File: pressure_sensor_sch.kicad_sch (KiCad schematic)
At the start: 54 parts, among them J13 1053131104, U7 ADS131M06IPBS

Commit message: Most Review 1 changes made
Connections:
- net GND: now also U7.22 (XTAL2)
- no-connect marks 3 -> 2
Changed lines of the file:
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@@
   (junction (at 221.996 125.984) (diameter 0) (color 0 0 0 0)
   )
-  (no_connect (at 98.298 106.68))
   (no_connect (at 98.298 116.84))
   (no_connect (at 32.258 114.3))
@@
         )
       )
+    )
+  )
+  (symbol (lib_name "GND_1") (lib_id "power:GND") (at 98.298 106.68 0) (unit 1)
+    (in_bom yes) (on_board yes) (dnp no) (fields_autoplaced)
+    (property "Reference" "#PWR0181" (at 98.298 113.03 0)
+      (effects (font (size 1.27 1.27)) hide)
+    )
+    (property "Value" "GND" (at 98.298 111.506 0)
+      (effects (font (size 1.27 1.27)) hide)
+    )
+    (property "Footprint" "" (at 98.298 106.68 0)
+      (effects (font (size 1.27 1.27)) hide)
+    )
+    (property "Datasheet" "" (at 98.298 106.68 0)
+      (effects (font (size 1.27 1.27)) hide)
+    )
+    (pin "1")
+    (instances
+      (project "Ricardo-Stark"
+        (path "/7db990e4-92e1-4f99-b4d2-435bbec1ba83/249a9f46-b59f-4de1-97d1-386ac76339a5"
+          (reference "#PWR0181") (unit 1)
+        )
+      )

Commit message: Review 1 Changes Complete
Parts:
- removed C39: 220nF, Capacitor_SMD:C_0402_1005Metric, symbol Device:C_Small
- removed C39: 1uF, Capacitor_SMD:C_0402_1005Metric, symbol Device:C_Small
- added C41: 0.1uF, Capacitor_SMD:C_0402_1005Metric, symbol Device:C_Small
- added C43: 220nF, Capacitor_SMD:C_0402_1005Metric, symbol Device:C_Small
- added C46: 1uF, Capacitor_SMD:C_0402_1005Metric, symbol Device:C_Small
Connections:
- net +3.3V: now also C41.1, C46.1
- net GND: now also C41.2, C43.2, C46.2
- net at U7.24 (CAP): now also C43.1
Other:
- moved on the sheet: JP39, R61

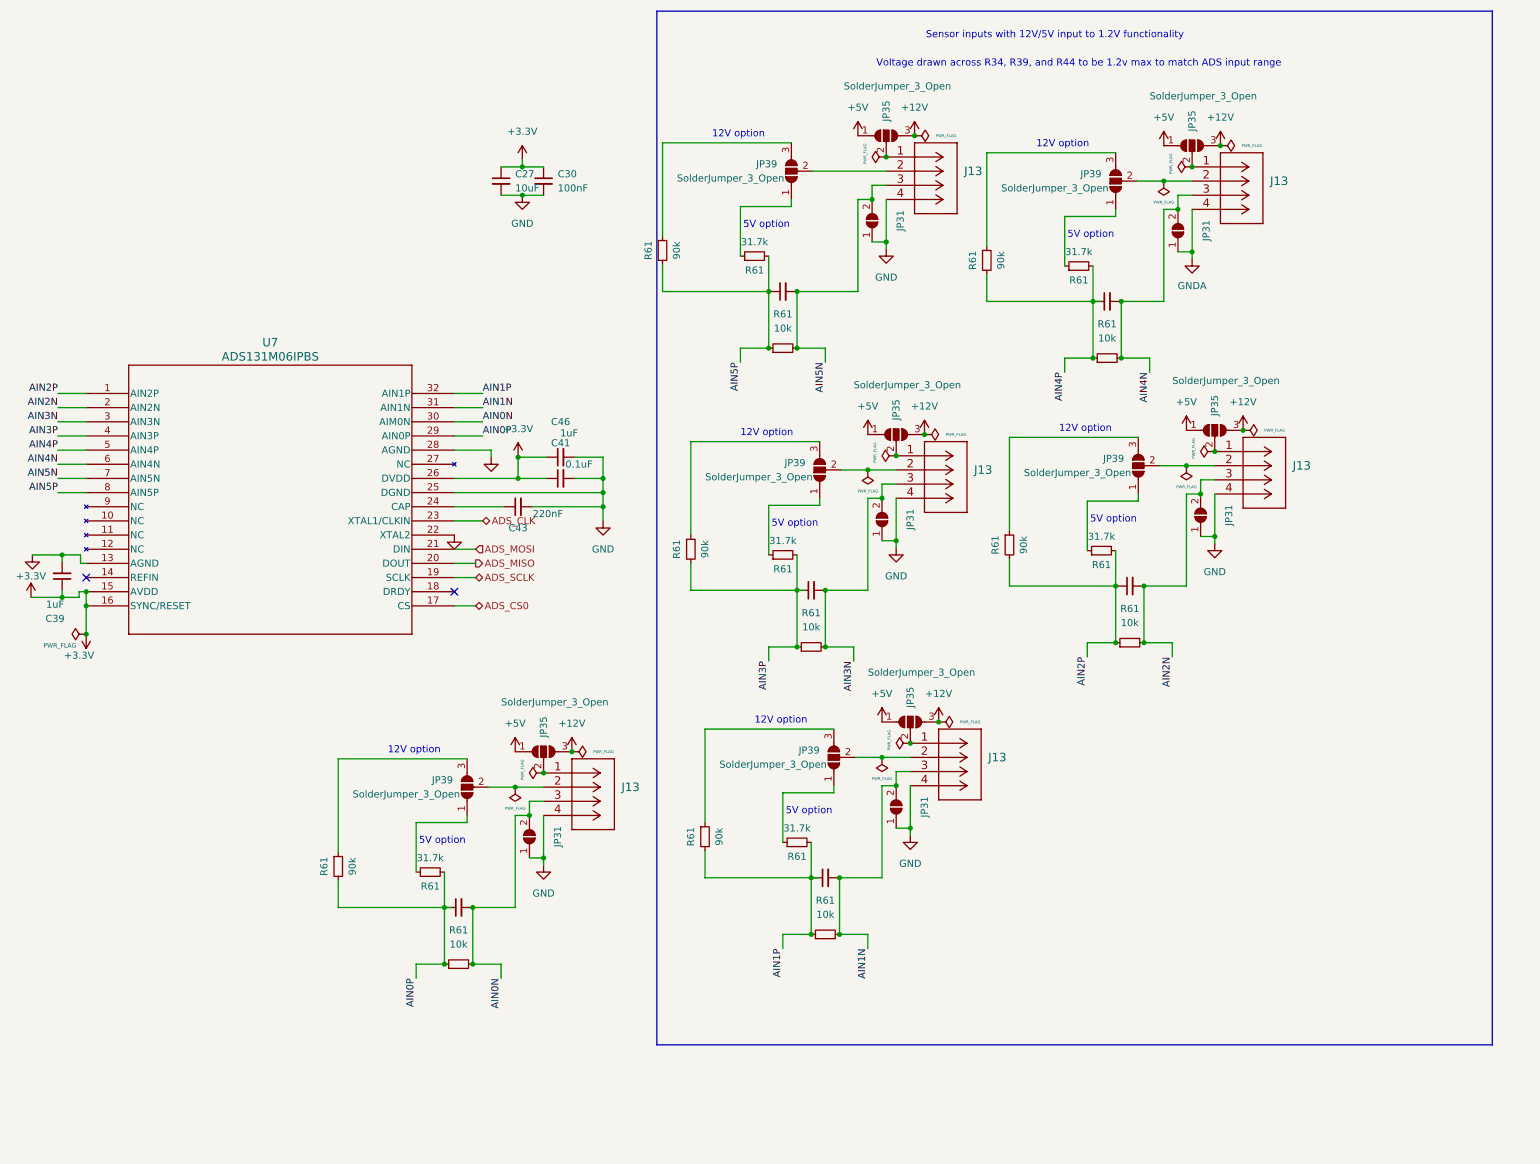
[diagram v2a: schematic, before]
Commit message: Sized sensor resistors and more routing
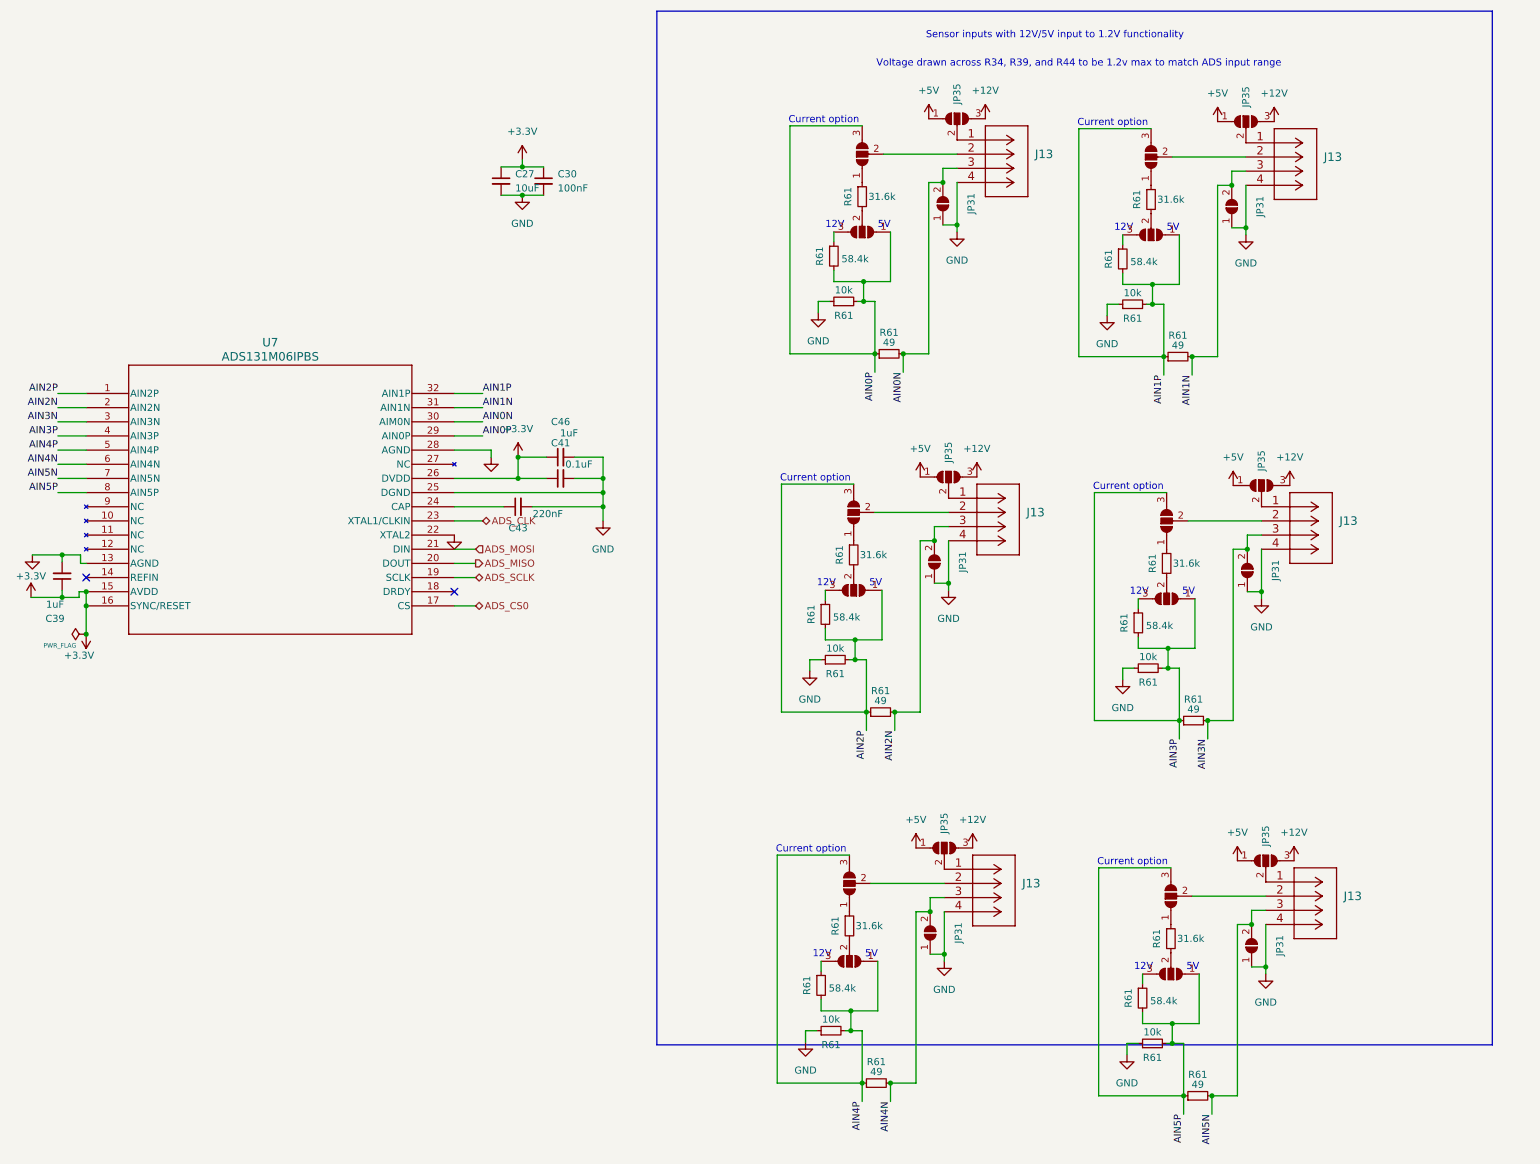
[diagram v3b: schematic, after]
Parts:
- removed C73 (x6): 10nF, Capacitor_SMD:C_0402_1005Metric, symbol Device:C_Small
- removed J13 (x5): 1053131104, Connector_Molex:Molex_Nano-Fit_105313-xx04_1x04_P2.50mm_Horizontal, symbol iclr:1053131104
- removed JP31 (x5): SolderJumper_2_Open, Jumper:SolderJumper-2_P1.3mm_Open_RoundedPad1.0x1.5mm, symbol Jumper:SolderJumper_2_Open
- removed JP35 (x5), JP39 (x5): SolderJumper_3_Open, Jumper:SolderJumper-3_P1.3mm_Open_RoundedPad1.0x1.5mm_NumberLabels, symbol Jumper:SolderJumper_3_Open
- removed R61 (x6): 31.7k, Resistor_SMD:R_0402_1005Metric, symbol Device:R_Small
- removed R61 (x6): 90k, Resistor_SMD:R_0402_1005Metric, symbol Device:R_Small
- removed R61 (x5): 10k, Resistor_SMD:R_0402_1005Metric, symbol Device:R_Small
- added J13 (x5): 1053131104, Connector_Molex:Molex_Nano-Fit_105313-xx04_1x04_P2.50mm_Horizontal, symbol iclr:1053131104
- added JP31 (x5): SolderJumper_2_Open, iclr:SmallerSolderJP, symbol Jumper:SolderJumper_2_Open
- added JP35 (x5), JP39 (x11): SolderJumper_3_Open, Jumper:SolderJumper-3_P1.3mm_Open_RoundedPad1.0x1.5mm_NumberLabels, symbol Jumper:SolderJumper_3_Open
- added R61 (x6): 31.6k, Resistor_SMD:R_0402_1005Metric, symbol Device:R_Small
- added R61 (x6): 10k, Resistor_SMD:R_0402_1005Metric, symbol Device:R_Small
- added R61 (x6): 58.4k, Resistor_SMD:R_0402_1005Metric, symbol Device:R_Small
- added R61 (x5): 49, Resistor_SMD:R_0402_1005Metric, symbol Device:R_Small
- JP31: footprint Jumper:SolderJumper-2_P1.3mm_Open_RoundedPad1.0x1.5mm -> iclr:SmallerSolderJP
- R61: value 10k -> 49
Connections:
- net +12V: now also JP35.3 (B), JP35.3 (B), JP35.3 (B), JP35.3 (B), JP35.3 (B)
- net +5V: now also JP35.1 (A), JP35.1 (A), JP35.1 (A), JP35.1 (A), JP35.1 (A)
- net AIN0N: now also J13.3, JP31.2 (B), R61.2
- net AIN0P: now also JP39.3 (B), R61.1, JP39.1 (A), R61.2, R61.2
- net AIN1N: now also J13.3, JP31.2 (B), R61.2
- net AIN1P: now also JP39.1 (A), JP39.3 (B), R61.1, R61.2, R61.2
- net AIN2N: now also J13.3, JP31.2 (B), R61.2
- net AIN2P: now also JP39.1 (A), JP39.3 (B), R61.1, R61.2, R61.2
- net AIN3N: now also J13.3, JP31.2 (B), R61.2
- net AIN3P: now also JP39.1 (A), JP39.3 (B), R61.1, R61.2, R61.2
- net AIN4N: now also J13.3, JP31.2 (B), R61.2
- net AIN4P: now also JP39.1 (A), JP39.3 (B), R61.1, R61.2, R61.2
- net AIN5N: now also J13.3, JP31.2 (B), R61.2; no longer J13.3, JP31.2 (B), R61.2
- net AIN5P: now also JP39.1 (A), JP39.3 (B), R61.1, R61.2, R61.2; no longer R61.1
- net GND: now also J13.4, J13.4, J13.4, J13.4, J13.4, JP31.1 (A), JP31.1 (A), JP31.1 (A), JP31.1 (A), JP31.1 (A), R61.1, R61.1, R61.1, R61.1, R61.1, R61.1
- net at JP39.1 (A): now also R61.1
- new net: JP39.1 (A), R61.1 (x5)
- new net: JP39.2 (C), R61.2 (x6)
- new net: J13.1, JP35.2 (C) (x5)
- new net: JP39.3 (B), R61.1 (x6)
- new net: J13.2, JP39.2 (C) (x5)
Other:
- note added: "12V"
- note added: "5V"
- note added: "Current option"
- note removed: "12V option"
- note removed: "5V option"
- moved on the sheet: J13, JP31, JP35, R61

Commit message: Commit
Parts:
- removed C27: 10uF, Capacitor_SMD:C_0603_1608Metric, symbol Device:C_Small
- removed C30: 100nF, Capacitor_SMD:C_0603_1608Metric, symbol Device:C_Small
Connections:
- net GND: now also U7.33 (GND)
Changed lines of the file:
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@@
 (kicad_sch (version 20230121) (generator eeschema)
   (paper "A4")
-  (junction (at 110.49 40.64) (diameter 0) (color 0 0 0 0)
-  )
   (junction (at 124.968 99.06) (diameter 0) (color 0 0 0 0)
   )
@@
   (junction (at 234.188 207.264) (diameter 0) (color 0 0 0 0)
   )
-  (junction (at 110.49 45.72) (diameter 0) (color 0 0 0 0)
-  )
   (junction (at 184.404 107.696) (diameter 0) (color 0 0 0 0)
   )
@@
     (stroke (width 0) (type default))
   )
-  (wire (pts (xy 110.49 40.64) (xy 114.3 40.64))
-    (stroke (width 0) (type default))
-  )
   (wire (pts (xy 233.426 139.954) (xy 233.426 143.256))
     (stroke (width 0) (type default))
@@
     (stroke (width 0) (type default))
   )
-  (wire (pts (xy 110.49 45.72) (xy 114.3 45.72))
-    (stroke (width 0) (type default))
-  )
   (wire (pts (xy 225.552 65.278) (xy 225.552 74.676))
     (stroke (width 0) (type default))
@@
     (stroke (width 0) (type default))
   )
-  (wire (pts (xy 106.68 40.64) (xy 110.49 40.64))
-    (stroke (width 0) (type default))
-  )
   (wire (pts (xy 231.14 127) (xy 231.14 118.11))
     (stroke (width 0) (type default))
   )
-  (wire (pts (xy 110.49 39.37) (xy 110.49 40.64))
-    (stroke (width 0) (type default))
-  )
   (polyline (pts (xy 134.62 12.7) (xy 284.48 12.7))
     (stroke (width 0) (type default))
@@
     (stroke (width 0) (type default))
   )
-  (wire (pts (xy 106.68 45.72) (xy 110.49 45.72))
-    (stroke (width 0) (type default))
-  )
   (wire (pts (xy 238.76 207.264) (xy 238.76 176.53))
     (stroke (width 0) (type default))
@@
     (pin "31")
     (pin "16")
+    (pin "33")
     (instances
       (project "Ricardo-Stark"
@@
     )
   )
-  (symbol (lib_id "power:GND") (at 110.49 45.72 0) (unit 1)
-    (in_bom yes) (on_board yes) (dnp no) (fields_autoplaced)
-    (property "Reference" "#PWR0151" (at 110.49 52.07 0)
-      (effects (font (size 1.27 1.27)) hide)
-    )
-    (property "Value" "GND" (at 110.49 50.8 0)
-      (effects (font (size 1.27 1.27)))
-    )
-    (property "Footprint" "" (at 110.49 45.72 0)
-      (effects (font (size 1.27 1.27)) hide)
-    )
-    (property "Datasheet" "" (at 110.49 45.72 0)
-      (effects (font (size 1.27 1.27)) hide)
-    )
-    (pin "1")
-    (instances
-      (project "sensorboard - Copy"
-        (path "/26801cfb-b53b-4a6a-a2f4-5f4986565765/00000000-0000-0000-0000-000061b9f0c0"
-          (reference "#PWR0151") (unit 1)
-        )
-      )
-      (project "Ricardo-Stark"
-        (path "/7db990e4-92e1-4f99-b4d2-435bbec1ba83/249a9f46-b59f-4de1-97d1-386ac76339a5"
-          (reference "#PWR093") (unit 1)
-        )
-      )
-    )
-  )
   (symbol (lib_name "+3.3V_1") (lib_id "power:+3.3V") (at 32.258 124.46 180) (unit 1)
     (in_bom yes) (on_board yes) (dnp no)
@@
     )
   )
-  (symbol (lib_id "Device:C_Small") (at 114.3 43.18 0) (unit 1)
-    (in_bom yes) (on_board yes) (dnp no) (fields_autoplaced)
-    (property "Reference" "C30" (at 116.84 41.9163 0)
-      (effects (font (size 1.27 1.27)) (justify left))
-    )
-    (property "Value" "100nF" (at 116.84 44.4563 0)
-      (effects (font (size 1.27 1.27)) (justify left))
-    )
-    (property "Footprint" "Capacitor_SMD:C_0603_1608Metric" (at 114.3 43.18 0)
-      (effects (font (size 1.27 1.27)) hide)
-    )
-    (property "Datasheet" "~" (at 114.3 43.18 0)
-      (effects (font (size 1.27 1.27)) hide)
-    )
-    (pin "1")
-    (pin "2")
-    (instances
-      (project "sensorboard - Copy"
-        (path "/26801cfb-b53b-4a6a-a2f4-5f4986565765/00000000-0000-0000-0000-000061b9f0c0"
-          (reference "C30") (unit 1)
-        )
-      )
-      (project "Ricardo-Stark"
-        (path "/7db990e4-92e1-4f99-b4d2-435bbec1ba83/249a9f46-b59f-4de1-97d1-386ac76339a5"
-          (reference "C42") (unit 1)
-        )
-      )
-    )
-  )
   (symbol (lib_id "power:+12V") (at 245.364 32.512 0) (unit 1)
     (in_bom yes) (on_board yes) (dnp no) (fields_autoplaced)
@@
     )
   )
-  (symbol (lib_id "Device:C_Small") (at 106.68 43.18 0) (unit 1)
-    (in_bom yes) (on_board yes) (dnp no) (fields_autoplaced)
-    (property "Reference" "C27" (at 109.22 41.9163 0)
-      (effects (font (size 1.27 1.27)) (justify left))
-    )
-    (property "Value" "10uF" (at 109.22 44.4563 0)
-      (effects (font (size 1.27 1.27)) (justify left))
-    )
-    (property "Footprint" "Capacitor_SMD:C_0603_1608Metric" (at 106.68 43.18 0)
-      (effects (font (size 1.27 1.27)) hide)
-    )
-    (property "Datasheet" "~" (at 106.68 43.18 0)
-      (effects (font (size 1.27 1.27)) hide)
-    )
-    (pin "1")
-    (pin "2")
-    (instances
-      (project "sensorboard - Copy"
-        (path "/26801cfb-b53b-4a6a-a2f4-5f4986565765/00000000-0000-0000-0000-000061b9f0c0"
-          (reference "C27") (unit 1)
-        )
-      )
-      (project "Ricardo-Stark"
-        (path "/7db990e4-92e1-4f99-b4d2-435bbec1ba83/249a9f46-b59f-4de1-97d1-386ac76339a5"
-          (reference "C41") (unit 1)
-        )
-      )
-    )
-  )
   (symbol (lib_id "Jumper:SolderJumper_2_Open") (at 184.404 111.506 90) (unit 1)
     (in_bom yes) (on_board yes) (dnp no)
@@
     )
   )
-  (symbol (lib_id "power:+3.3V") (at 110.49 39.37 0) (unit 1)
-    (in_bom yes) (on_board yes) (dnp no) (fields_autoplaced)
-    (property "Reference" "#PWR0150" (at 110.49 43.18 0)
-      (effects (font (size 1.27 1.27)) hide)
-    )
-    (property "Value" "+3.3V" (at 110.49 34.29 0)
-      (effects (font (size 1.27 1.27)))
-    )
-    (property "Footprint" "" (at 110.49 39.37 0)
-      (effects (font (size 1.27 1.27)) hide)
-    )
-    (property "Datasheet" "" (at 110.49 39.37 0)
-      (effects (font (size 1.27 1.27)) hide)
-    )
-    (pin "1")
-    (instances
-      (project "sensorboard - Copy"
-        (path "/26801cfb-b53b-4a6a-a2f4-5f4986565765/00000000-0000-0000-0000-000061b9f0c0"
-          (reference "#PWR0150") (unit 1)
-        )
-      )
-      (project "Ricardo-Stark"
-        (path "/7db990e4-92e1-4f99-b4d2-435bbec1ba83/249a9f46-b59f-4de1-97d1-386ac76339a5"
-          (reference "#PWR092") (unit 1)
-        )
-      )
-    )
-  )
   (symbol (lib_id "Jumper:SolderJumper_2_Open") (at 241.3 180.34 90) (unit 1)
     (in_bom yes) (on_board yes) (dnp no)
@@
         )
       )
+    )
+  )
+  (symbol (lib_name "GND_1") (lib_id "power:GND") (at 98.298 78.74 0) (unit 1)
+    (in_bom yes) (on_board yes) (dnp no) (fields_autoplaced)
+    (property "Reference" "#PWR091" (at 98.298 85.09 0)
+      (effects (font (size 1.27 1.27)) hide)
+    )
+    (property "Value" "GND" (at 98.298 83.566 0)
+      (effects (font (size 1.27 1.27)) hide)
+    )
+    (property "Footprint" "" (at 98.298 78.74 0)
+      (effects (font (size 1.27 1.27)) hide)
+    )
+    (property "Datasheet" "" (at 98.298 78.74 0)
+      (effects (font (size 1.27 1.27)) hide)
+    )
+    (pin "1")
+    (instances
+      (project "Ricardo-Stark"
+        (path "/7db990e4-92e1-4f99-b4d2-435bbec1ba83/249a9f46-b59f-4de1-97d1-386ac76339a5"
+          (reference "#PWR091") (unit 1)
+        )
+      )

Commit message: commit
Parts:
- removed R61: 49, Resistor_SMD:R_0402_1005Metric, symbol Device:R_Small
- added C33: 10nF, Capacitor_SMD:C_0402_1005Metric, symbol Device:C_Small
- added JP4: SolderJumper_2_Open, iclr:SmallerSolderJP, symbol Jumper:SolderJumper_2_Open
- added R46, R47: 1k, Resistor_SMD:R_0402_1005Metric, symbol Device:R_Small
- added R49: 49, Resistor_SMD:R_0402_1005Metric, symbol Device:R_Small
- R61: value 58.4k -> 14k
- R61: value 31.6k -> 75k
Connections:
- net AIN0N: now also C33.1, R46.1; no longer J13.3, JP31.2 (B)
- net AIN0P: now also C33.2, R47.1; no longer JP39.1 (A), JP39.3 (B), R61.2, R61.2
- net GND: now also R61.2; no longer R61.1
- net at JP39.1 (A): now also JP39.2 (C), JP4.2 (B), R46.2; no longer R61.1
- net at JP39.3 (B), R61.1: now also R61.2
- new net: J13.3, JP31.2 (B), R47.2, R49.1
- new net: JP39.1 (A), R61.1, R61.2
- new net: JP39.3 (B), R61.1
- new net: JP4.1 (A), R49.2
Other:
- note added: "Volatge option"
- moved on the sheet: R61
